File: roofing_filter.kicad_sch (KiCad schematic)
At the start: 9 parts, among them Y2001 45.1 MHz, Y2002 45.1 MHz

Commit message: Update pcb database to version 6
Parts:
- C2001, C2003: symbol Custom:C_US -> custom:C_US; PartNumber 800239-160 -> 800063-XXX
- C2002: symbol Custom:C_US -> custom:C_US; PartNumber 800239-130 -> 800063-XXX
- R2001, R2002: symbol Custom:R_US -> custom:R_US; PartNumber 800235-000 -> 800XXX-XXX
- Y2001, Y2002: symbol Custom:Monolithic_Crystal_Filter_2P -> custom:Monolithic_Crystal_Filter_2P; PartNumber 800287-101 -> 800XXX-XXX
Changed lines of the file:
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@@
     (pin "2")
   )
-  (symbol (lib_id "Custom:C_US") (at 85.09 92.71 0) (unit 1)
+  (symbol (lib_id "custom:C_US") (at 85.09 92.71 0) (unit 1)
     (in_bom yes) (on_board yes)
     (property "Reference" "C2001" (id 0) (at 88.392 91.5416 0)
@@
       (effects (font (size 1.524 1.524)))
     )
-    (property "PartNumber" "800239-160" (id 4) (at 85.09 78.74 0)
-      (effects (font (size 1.524 1.524)) hide)
-    )
-    (pin "1")
-    (pin "2")
-  )
-  (symbol (lib_id "Custom:C_US") (at 212.09 92.71 0) (unit 1)
+    (property "PartNumber" "800063-XXX" (id 4) (at 85.09 78.74 0)
+      (effects (font (size 1.524 1.524)) hide)
+    )
+    (pin "1")
+    (pin "2")
+  )
+  (symbol (lib_id "custom:C_US") (at 212.09 92.71 0) (unit 1)
     (in_bom yes) (on_board yes)
     (property "Reference" "C2003" (id 0) (at 215.392 91.5416 0)
@@
       (effects (font (size 1.524 1.524)))
     )
-    (property "PartNumber" "800239-160" (id 4) (at 212.09 78.74 0)
-      (effects (font (size 1.524 1.524)) hide)
-    )
-    (pin "1")
-    (pin "2")
-  )
-  (symbol (lib_id "Custom:GND_US") (at 212.09 100.33 0) (unit 1)
+    (property "PartNumber" "800063-XXX" (id 4) (at 212.09 78.74 0)
+      (effects (font (size 1.524 1.524)) hide)
+    )
+    (pin "1")
+    (pin "2")
+  )
+  (symbol (lib_id "custom:GND_US") (at 212.09 100.33 0) (unit 1)
     (in_bom yes) (on_board yes)
     (property "Reference" "#PWR02005" (id 0) (at 211.582 103.632 0)
@@
     (pin "1")
   )
-  (symbol (lib_id "Custom:GND_US") (at 85.09 100.33 0) (unit 1)
+  (symbol (lib_id "custom:GND_US") (at 85.09 100.33 0) (unit 1)
     (in_bom yes) (on_board yes)
     (property "Reference" "#PWR02001" (id 0) (at 84.582 103.632 0)
@@
     (pin "1")
   )
-  (symbol (lib_id "Custom:Monolithic_Crystal_Filter_2P") (at 125.73 87.63 0) (unit 1)
+  (symbol (lib_id "custom:Monolithic_Crystal_Filter_2P") (at 125.73 87.63 0) (unit 1)
     (in_bom yes) (on_board yes)
     (property "Reference" "Y2001" (id 0) (at 125.73 80.899 0))
@@
       (effects (font (size 1.27 1.27)) hide)
     )
-    (property "PartNumber" "800287-101" (id 4) (at 116.84 95.25 0)
+    (property "PartNumber" "800XXX-XXX" (id 4) (at 116.84 95.25 0)
       (effects (font (size 1.27 1.27)) hide)
     )
@@
     (pin "3")
   )
-  (symbol (lib_id "Custom:Monolithic_Crystal_Filter_2P") (at 168.91 87.63 0) (mirror y) (unit 1)
+  (symbol (lib_id "custom:Monolithic_Crystal_Filter_2P") (at 168.91 87.63 0) (mirror y) (unit 1)
     (in_bom yes) (on_board yes)
     (property "Reference" "Y2002" (id 0) (at 168.91 80.899 0))
@@
       (effects (font (size 1.27 1.27)) hide)
     )
-    (property "PartNumber" "800287-101" (id 4) (at 177.8 95.25 0)
+    (property "PartNumber" "800XXX-XXX" (id 4) (at 177.8 95.25 0)
       (effects (font (size 1.27 1.27)) hide)
     )
@@
     (pin "3")
   )
-  (symbol (lib_id "Custom:GND_US") (at 125.73 100.33 0) (unit 1)
+  (symbol (lib_id "custom:GND_US") (at 125.73 100.33 0) (unit 1)
     (in_bom yes) (on_board yes)
     (property "Reference" "#PWR02002" (id 0) (at 125.222 103.632 0)
@@
     (pin "1")
   )
-  (symbol (lib_id "Custom:GND_US") (at 168.91 100.33 0) (unit 1)
+  (symbol (lib_id "custom:GND_US") (at 168.91 100.33 0) (unit 1)
     (in_bom yes) (on_board yes)
     (property "Reference" "#PWR02004" (id 0) (at 168.402 103.632 0)
@@
     (pin "1")
   )
-  (symbol (lib_id "Custom:C_US") (at 147.32 92.71 0) (unit 1)
+  (symbol (lib_id "custom:C_US") (at 147.32 92.71 0) (unit 1)
     (in_bom yes) (on_board yes)
     (property "Reference" "C2002" (id 0) (at 150.622 91.5416 0)
@@
       (effects (font (size 1.524 1.524)))
     )
-    (property "PartNumber" "800239-130" (id 4) (at 147.32 78.74 0)
-      (effects (font (size 1.524 1.524)) hide)
-    )
-    (pin "1")
-    (pin "2")
-  )
-  (symbol (lib_id "Custom:GND_US") (at 147.32 100.33 0) (unit 1)
+    (property "PartNumber" "800063-XXX" (id 4) (at 147.32 78.74 0)
+      (effects (font (size 1.524 1.524)) hide)
+    )
+    (pin "1")
+    (pin "2")
+  )
+  (symbol (lib_id "custom:GND_US") (at 147.32 100.33 0) (unit 1)
     (in_bom yes) (on_board yes)
     (property "Reference" "#PWR02003" (id 0) (at 146.812 103.632 0)
@@
     (pin "1")
   )
-  (symbol (lib_id "Custom:R_US") (at 38.1 86.36 270) (unit 1)
+  (symbol (lib_id "custom:R_US") (at 38.1 86.36 270) (unit 1)
     (in_bom yes) (on_board yes)
     (property "Reference" "R2001" (id 0) (at 38.1 81.3562 90))
@@
       (effects (font (size 1.524 1.524)))
     )
-    (property "PartNumber" "800235-000" (id 4) (at 40.64 90.932 90)
-      (effects (font (size 1.524 1.524)) hide)
-    )
-    (pin "1")
-    (pin "2")
-  )
-  (symbol (lib_id "Custom:R_US") (at 255.27 86.36 270) (unit 1)
+    (property "PartNumber" "800XXX-XXX" (id 4) (at 40.64 90.932 90)
+      (effects (font (size 1.524 1.524)) hide)
+    )
+    (pin "1")
+    (pin "2")
+  )
+  (symbol (lib_id "custom:R_US") (at 255.27 86.36 270) (unit 1)
     (in_bom yes) (on_board yes)
     (property "Reference" "R2002" (id 0) (at 255.27 81.3562 90))
@@
       (effects (font (size 1.524 1.524)))
     )
-    (property "PartNumber" "800235-000" (id 4) (at 257.81 90.932 90)
-      (effects (font (size 1.524 1.524)) hide)
-    )
+    (property "PartNumber" "800XXX-XXX" (id 4) (at 257.81 90.932 90)
+      (effects (font (size 1.524 1.524)) hide)
+    )

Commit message: Fix BOM part number errors and out of sync footprints which happened during conversion from Kicad 5 to 6
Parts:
- C2001, C2003: PartNumber 800063-XXX -> 800239-160
- C2002: PartNumber 800063-XXX -> 800239-130
- R2001, R2002: PartNumber 800XXX-XXX -> 800235-000
- Y2001, Y2002: PartNumber 800XXX-XXX -> 800287-101
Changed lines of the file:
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@@
       (effects (font (size 1.524 1.524)))
     )
-    (property "PartNumber" "800063-XXX" (id 4) (at 85.09 78.74 0)
+    (property "PartNumber" "800239-160" (id 4) (at 85.09 78.74 0)
       (effects (font (size 1.524 1.524)) hide)
     )
@@
       (effects (font (size 1.524 1.524)))
     )
-    (property "PartNumber" "800063-XXX" (id 4) (at 212.09 78.74 0)
+    (property "PartNumber" "800239-160" (id 4) (at 212.09 78.74 0)
       (effects (font (size 1.524 1.524)) hide)
     )
@@
       (effects (font (size 1.27 1.27)) hide)
     )
-    (property "PartNumber" "800XXX-XXX" (id 4) (at 116.84 95.25 0)
+    (property "PartNumber" "800287-101" (id 4) (at 116.84 95.25 0)
       (effects (font (size 1.27 1.27)) hide)
     )
@@
       (effects (font (size 1.27 1.27)) hide)
     )
-    (property "PartNumber" "800XXX-XXX" (id 4) (at 177.8 95.25 0)
+    (property "PartNumber" "800287-101" (id 4) (at 177.8 95.25 0)
       (effects (font (size 1.27 1.27)) hide)
     )
@@
       (effects (font (size 1.524 1.524)))
     )
-    (property "PartNumber" "800063-XXX" (id 4) (at 147.32 78.74 0)
+    (property "PartNumber" "800239-130" (id 4) (at 147.32 78.74 0)
       (effects (font (size 1.524 1.524)) hide)
     )
@@
       (effects (font (size 1.524 1.524)))
     )
-    (property "PartNumber" "800XXX-XXX" (id 4) (at 40.64 90.932 90)
+    (property "PartNumber" "800235-000" (id 4) (at 40.64 90.932 90)
       (effects (font (size 1.524 1.524)) hide)
     )
@@
       (effects (font (size 1.524 1.524)))
     )
-    (property "PartNumber" "800XXX-XXX" (id 4) (at 257.81 90.932 90)
+    (property "PartNumber" "800235-000" (id 4) (at 257.81 90.932 90)
       (effects (font (size 1.524 1.524)) hide)
     )

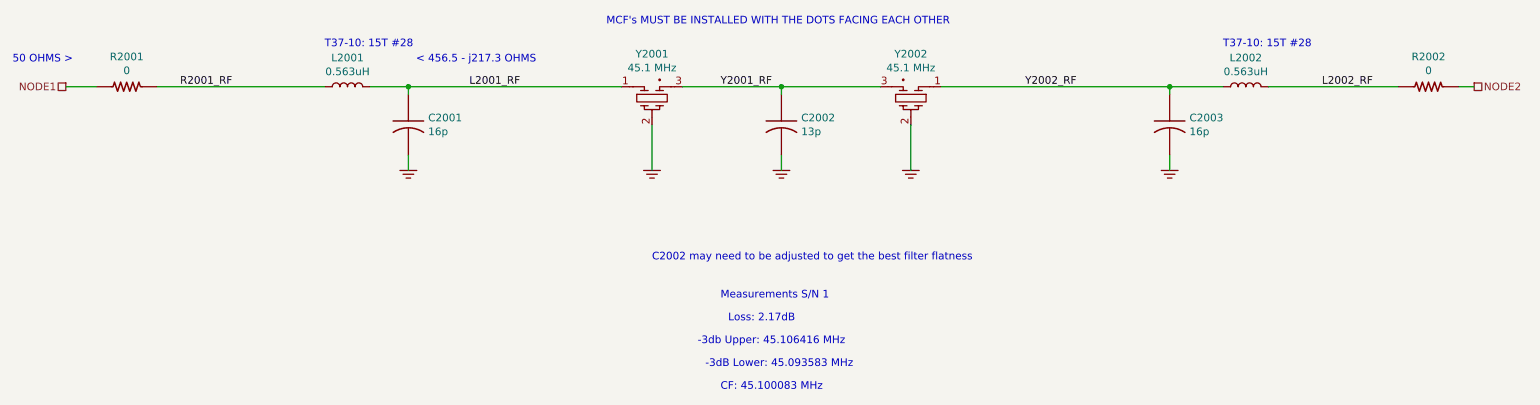
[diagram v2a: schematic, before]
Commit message: trx_mobo_concept_2_B. Change design to use a dedicated 8V supply for the 2SC3357 parts. Add S-Meter connector. Change mic connector to 3 pins and add 8V sopower supply to pin 3.
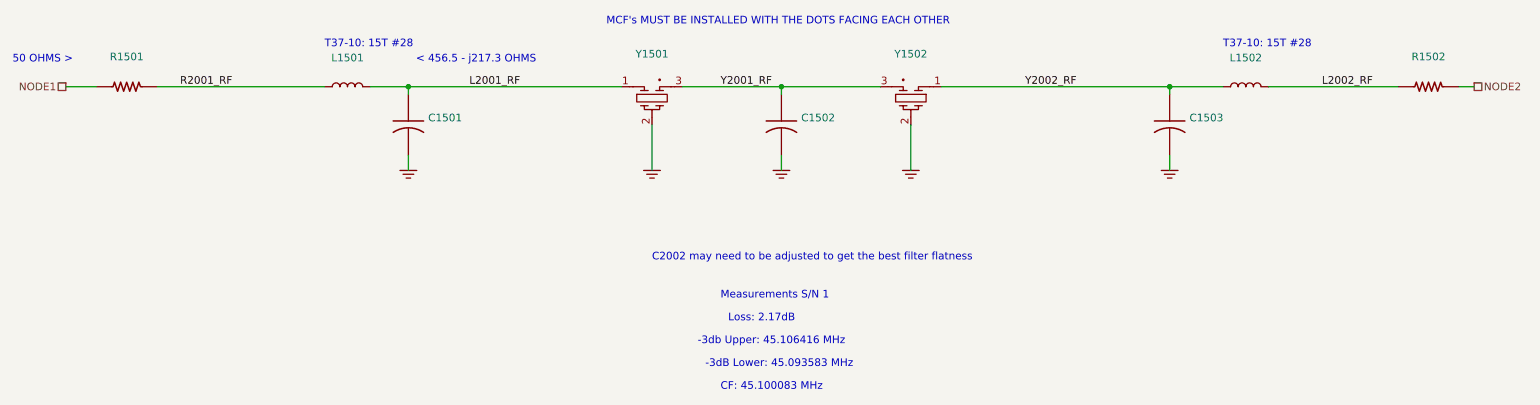
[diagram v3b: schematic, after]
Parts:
- C1501: renamed from C2001; value 16p -> (none); footprint Capacitor_SMD:C_0805_2012Metric_Pad1.15x1.40mm_HandSolder -> (none)
- C1502: renamed from C2002; value 13p -> (none); footprint Capacitor_SMD:C_0805_2012Metric_Pad1.15x1.40mm_HandSolder -> (none)
- C1503: renamed from C2003; value 16p -> (none); footprint Capacitor_SMD:C_0805_2012Metric_Pad1.15x1.40mm_HandSolder -> (none)
- L1501: renamed from L2001; value 0.563uH -> (none); footprint mods:TOROID_T37_VERT -> (none)
- L1502: renamed from L2002; value 0.563uH -> (none); footprint mods:TOROID_T37_VERT -> (none)
- R1501: renamed from R2001; value 0 -> (none); footprint Resistor_SMD:R_0805_2012Metric_Pad1.15x1.40mm_HandSolder -> (none)
- R1502: renamed from R2002; value 0 -> (none); footprint Resistor_SMD:R_0805_2012Metric_Pad1.15x1.40mm_HandSolder -> (none)
- Y1501: renamed from Y2001; value 45.1 MHz -> (none); footprint mods:MCF-1.875_7.8x3.2 -> (none)
- Y1502: renamed from Y2002; value 45.1 MHz -> (none); footprint mods:MCF-1.875_7.8x3.2 -> (none)
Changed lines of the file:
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@@
   (title_block
     (title "ROOFING FILTER")
-    (rev "X1")
+    (rev "B")
   )
   (junction (at 212.09 86.36) (diameter 0) (color 0 0 0 0)
@@
   (symbol (lib_id "Device:L") (at 74.93 86.36 90) (unit 1)
     (in_bom yes) (on_board yes)
-    (property "Reference" "L2001" (id 0) (at 74.93 81.534 90))
-    (property "Value" "0.563uH" (id 1) (at 74.93 83.8454 90))
-    (property "Footprint" "mods:TOROID_T37_VERT" (id 2) (at 74.93 86.36 0)
+    (property "Reference" "L1501" (id 0) (at 74.93 81.534 90))
+    (property "Value" "" (id 1) (at 74.93 83.8454 90))
+    (property "Footprint" "" (id 2) (at 74.93 86.36 0)
       (effects (font (size 1.27 1.27)) hide)
     )
@@
   (symbol (lib_id "Device:L") (at 224.79 86.36 90) (unit 1)
     (in_bom yes) (on_board yes)
-    (property "Reference" "L2002" (id 0) (at 224.79 81.534 90))
-    (property "Value" "0.563uH" (id 1) (at 224.79 83.8454 90))
-    (property "Footprint" "mods:TOROID_T37_VERT" (id 2) (at 224.79 86.36 0)
+    (property "Reference" "L1502" (id 0) (at 224.79 81.534 90))
+    (property "Value" "" (id 1) (at 224.79 83.8454 90))
+    (property "Footprint" "" (id 2) (at 224.79 86.36 0)
       (effects (font (size 1.27 1.27)) hide)
     )
@@
   (symbol (lib_id "custom:C_US") (at 85.09 92.71 0) (unit 1)
     (in_bom yes) (on_board yes)
-    (property "Reference" "C2001" (id 0) (at 88.392 91.5416 0)
-      (effects (font (size 1.27 1.27)) (justify left))
-    )
-    (property "Value" "16p" (id 1) (at 88.392 93.853 0)
-      (effects (font (size 1.27 1.27)) (justify left))
-    )
-    (property "Footprint" "Capacitor_SMD:C_0805_2012Metric_Pad1.15x1.40mm_HandSolder" (id 2) (at 87.63 81.28 0)
+    (property "Reference" "C1501" (id 0) (at 88.392 91.5416 0)
+      (effects (font (size 1.27 1.27)) (justify left))
+    )
+    (property "Value" "" (id 1) (at 88.392 93.853 0)
+      (effects (font (size 1.27 1.27)) (justify left))
+    )
+    (property "Footprint" "" (id 2) (at 87.63 81.28 0)
       (effects (font (size 1.524 1.524)) hide)
     )
@@
   (symbol (lib_id "custom:C_US") (at 212.09 92.71 0) (unit 1)
     (in_bom yes) (on_board yes)
-    (property "Reference" "C2003" (id 0) (at 215.392 91.5416 0)
-      (effects (font (size 1.27 1.27)) (justify left))
-    )
-    (property "Value" "16p" (id 1) (at 215.392 93.853 0)
-      (effects (font (size 1.27 1.27)) (justify left))
-    )
-    (property "Footprint" "Capacitor_SMD:C_0805_2012Metric_Pad1.15x1.40mm_HandSolder" (id 2) (at 214.63 81.28 0)
+    (property "Reference" "C1503" (id 0) (at 215.392 91.5416 0)
+      (effects (font (size 1.27 1.27)) (justify left))
+    )
+    (property "Value" "" (id 1) (at 215.392 93.853 0)
+      (effects (font (size 1.27 1.27)) (justify left))
+    )
+    (property "Footprint" "" (id 2) (at 214.63 81.28 0)
       (effects (font (size 1.524 1.524)) hide)
     )
@@
   (symbol (lib_id "custom:GND_US") (at 212.09 100.33 0) (unit 1)
     (in_bom yes) (on_board yes)
-    (property "Reference" "#PWR02005" (id 0) (at 211.582 103.632 0)
+    (property "Reference" "#PWR01505" (id 0) (at 211.582 103.632 0)
       (effects (font (size 0.762 0.762)) hide)
     )
@@
   (symbol (lib_id "custom:GND_US") (at 85.09 100.33 0) (unit 1)
     (in_bom yes) (on_board yes)
-    (property "Reference" "#PWR02001" (id 0) (at 84.582 103.632 0)
+    (property "Reference" "#PWR01501" (id 0) (at 84.582 103.632 0)
       (effects (font (size 0.762 0.762)) hide)
     )
@@
   (symbol (lib_id "custom:Monolithic_Crystal_Filter_2P") (at 125.73 87.63 0) (unit 1)
     (in_bom yes) (on_board yes)
-    (property "Reference" "Y2001" (id 0) (at 125.73 80.899 0))
-    (property "Value" "45.1 MHz" (id 1) (at 125.73 83.2104 0))
-    (property "Footprint" "mods:MCF-1.875_7.8x3.2" (id 2) (at 125.73 87.63 0)
+    (property "Reference" "Y1501" (id 0) (at 125.73 80.899 0))
+    (property "Value" "" (id 1) (at 125.73 83.2104 0))
+    (property "Footprint" "" (id 2) (at 125.73 87.63 0)
       (effects (font (size 1.27 1.27)) hide)
     )
@@
   (symbol (lib_id "custom:Monolithic_Crystal_Filter_2P") (at 168.91 87.63 0) (mirror y) (unit 1)
     (in_bom yes) (on_board yes)
-    (property "Reference" "Y2002" (id 0) (at 168.91 80.899 0))
-    (property "Value" "45.1 MHz" (id 1) (at 168.91 83.2104 0))
-    (property "Footprint" "mods:MCF-1.875_7.8x3.2" (id 2) (at 168.91 87.63 0)
+    (property "Reference" "Y1502" (id 0) (at 168.91 80.899 0))
+    (property "Value" "" (id 1) (at 168.91 83.2104 0))
+    (property "Footprint" "" (id 2) (at 168.91 87.63 0)
       (effects (font (size 1.27 1.27)) hide)
     )
@@
   (symbol (lib_id "custom:GND_US") (at 125.73 100.33 0) (unit 1)
     (in_bom yes) (on_board yes)
-    (property "Reference" "#PWR02002" (id 0) (at 125.222 103.632 0)
+    (property "Reference" "#PWR01502" (id 0) (at 125.222 103.632 0)
       (effects (font (size 0.762 0.762)) hide)
     )
@@
   (symbol (lib_id "custom:GND_US") (at 168.91 100.33 0) (unit 1)
     (in_bom yes) (on_board yes)
-    (property "Reference" "#PWR02004" (id 0) (at 168.402 103.632 0)
+    (property "Reference" "#PWR01504" (id 0) (at 168.402 103.632 0)
       (effects (font (size 0.762 0.762)) hide)
     )
@@
   (symbol (lib_id "custom:C_US") (at 147.32 92.71 0) (unit 1)
     (in_bom yes) (on_board yes)
-    (property "Reference" "C2002" (id 0) (at 150.622 91.5416 0)
-      (effects (font (size 1.27 1.27)) (justify left))
-    )
-    (property "Value" "13p" (id 1) (at 150.622 93.853 0)
-      (effects (font (size 1.27 1.27)) (justify left))
-    )
-    (property "Footprint" "Capacitor_SMD:C_0805_2012Metric_Pad1.15x1.40mm_HandSolder" (id 2) (at 149.86 81.28 0)
+    (property "Reference" "C1502" (id 0) (at 150.622 91.5416 0)
+      (effects (font (size 1.27 1.27)) (justify left))
+    )
+    (property "Value" "" (id 1) (at 150.622 93.853 0)
+      (effects (font (size 1.27 1.27)) (justify left))
+    )
+    (property "Footprint" "" (id 2) (at 149.86 81.28 0)
       (effects (font (size 1.524 1.524)) hide)
     )
@@
   (symbol (lib_id "custom:GND_US") (at 147.32 100.33 0) (unit 1)
     (in_bom yes) (on_board yes)
-    (property "Reference" "#PWR02003" (id 0) (at 146.812 103.632 0)
+    (property "Reference" "#PWR01503" (id 0) (at 146.812 103.632 0)
       (effects (font (size 0.762 0.762)) hide)
     )
@@
   (symbol (lib_id "custom:R_US") (at 38.1 86.36 270) (unit 1)
     (in_bom yes) (on_board yes)
-    (property "Reference" "R2001" (id 0) (at 38.1 81.3562 90))
-    (property "Value" "0" (id 1) (at 38.1 83.6676 90))
-    (property "Footprint" "Resistor_SMD:R_0805_2012Metric_Pad1.15x1.40mm_HandSolder" (id 2) (at 38.1 86.36 0)
+    (property "Reference" "R1501" (id 0) (at 38.1 81.3562 90))
+    (property "Value" "" (id 1) (at 38.1 83.6676 90))
+    (property "Footprint" "" (id 2) (at 38.1 86.36 0)
       (effects (font (size 1.524 1.524)) hide)
     )
@@
   (symbol (lib_id "custom:R_US") (at 255.27 86.36 270) (unit 1)
     (in_bom yes) (on_board yes)
-    (property "Reference" "R2002" (id 0) (at 255.27 81.3562 90))
-    (property "Value" "0" (id 1) (at 255.27 83.6676 90))
-    (property "Footprint" "Resistor_SMD:R_0805_2012Metric_Pad1.15x1.40mm_HandSolder" (id 2) (at 255.27 86.36 0)
-      (effects (font (size 1.524 1.524)) hide)
-    )
+    (property "Reference" "R1502" (id 0) (at 255.27 81.3562 90))
+    (property "Value" "" (id 1) (at 255.27 83.6676 90))
+    (property "Footprint" "" (id 2) (at 255.27 86.36 0)
+      (effects (font (size 1.524 1.524)) hide)
+    )
